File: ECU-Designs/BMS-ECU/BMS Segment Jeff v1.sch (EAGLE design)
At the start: 90 parts, among them Q10 P-CHANNEL_MOSFET_DMP3099L-7, Q11 P-CHANNEL_MOSFET_DMP3099L-7, Q12 P-CHANNEL_MOSFET_DMP3099L-7, Q13 NPN_BCP56T1, Q3 P-CHANNEL_MOSFET_DMP3099L-7, Q4 P-CHANNEL_MOSFET_DMP3099L-7, Q5 P-CHANNEL_MOSFET_DMP3099L-7, Q6 P-CHANNEL_MOSFET_DMP3099L-7, Q8 P-CHANNEL_MOSFET_DMP3099L-7, Q9 P-CHANNEL_MOSFET_DMP3099L-7

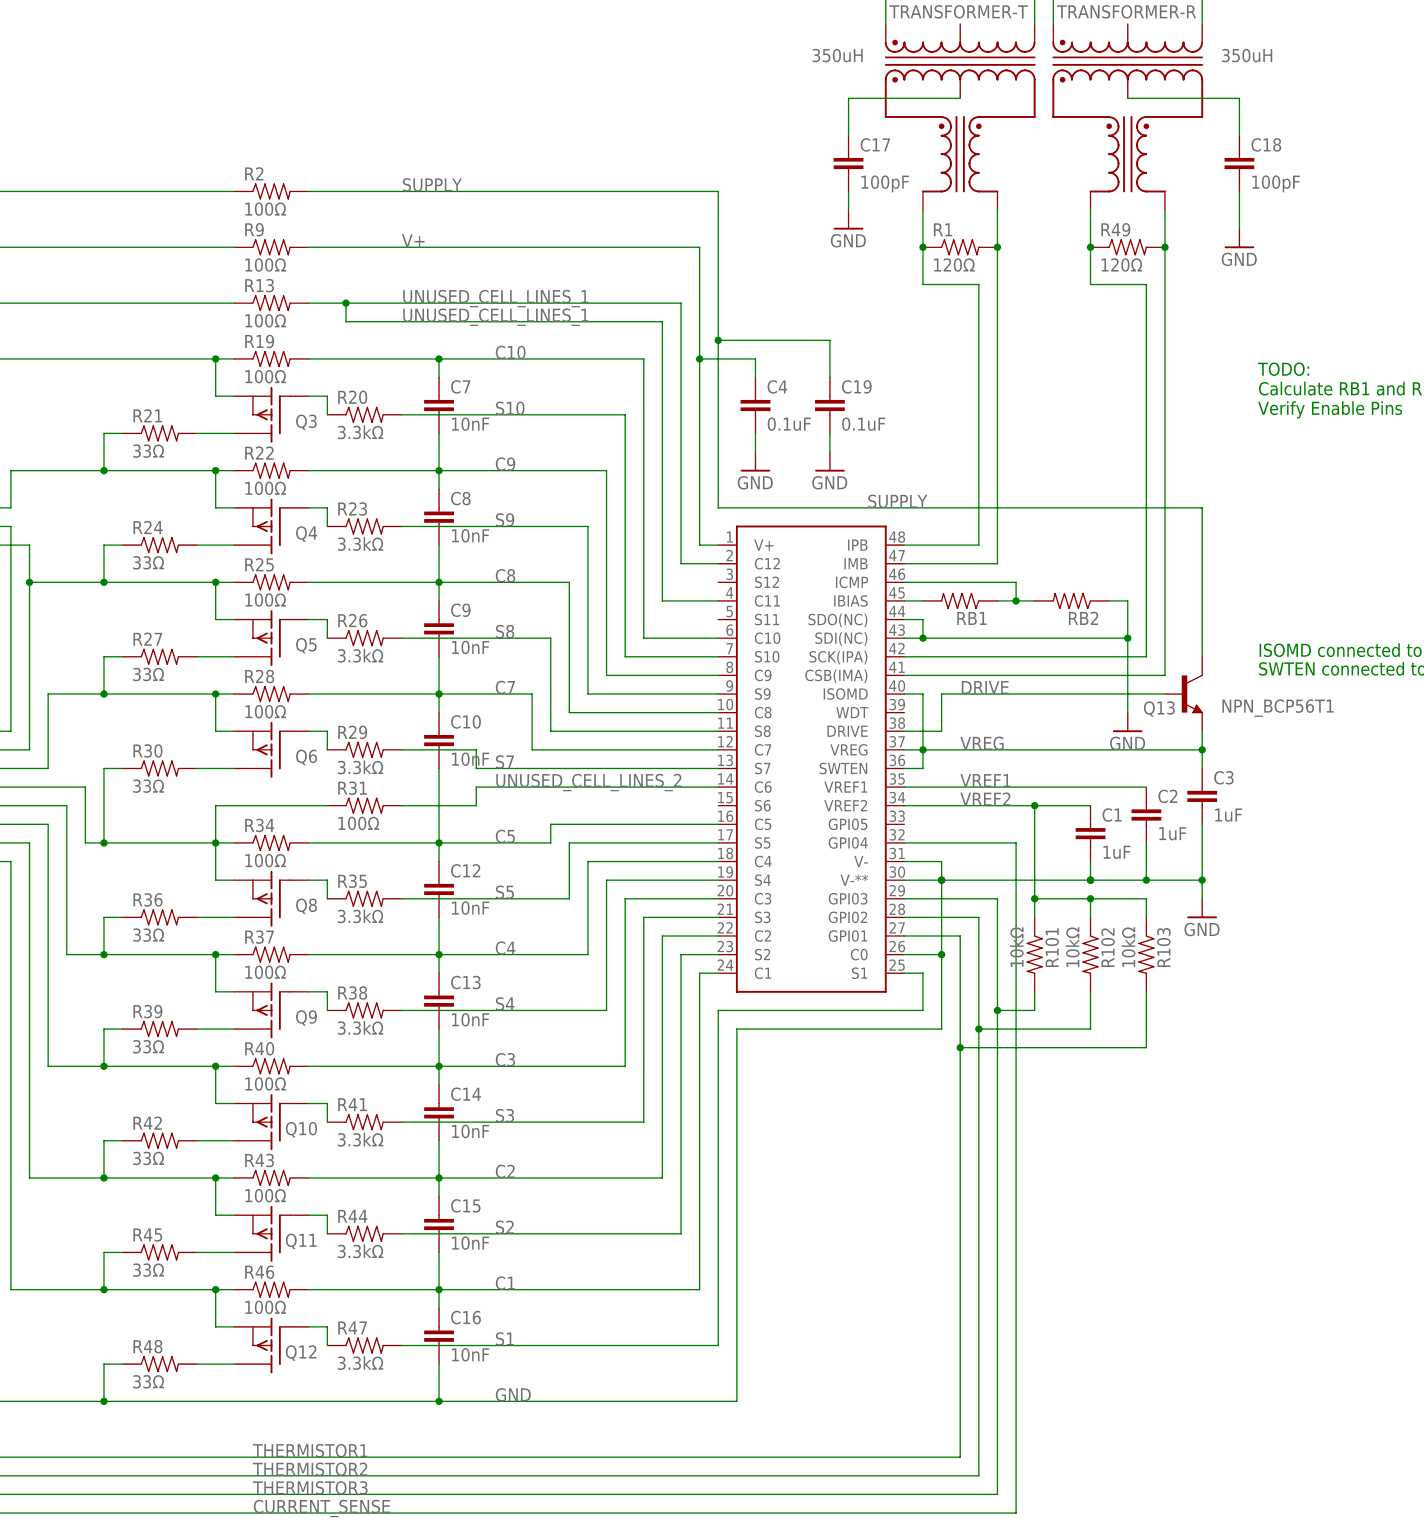
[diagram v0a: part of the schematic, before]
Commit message: Renamed components in increasing order
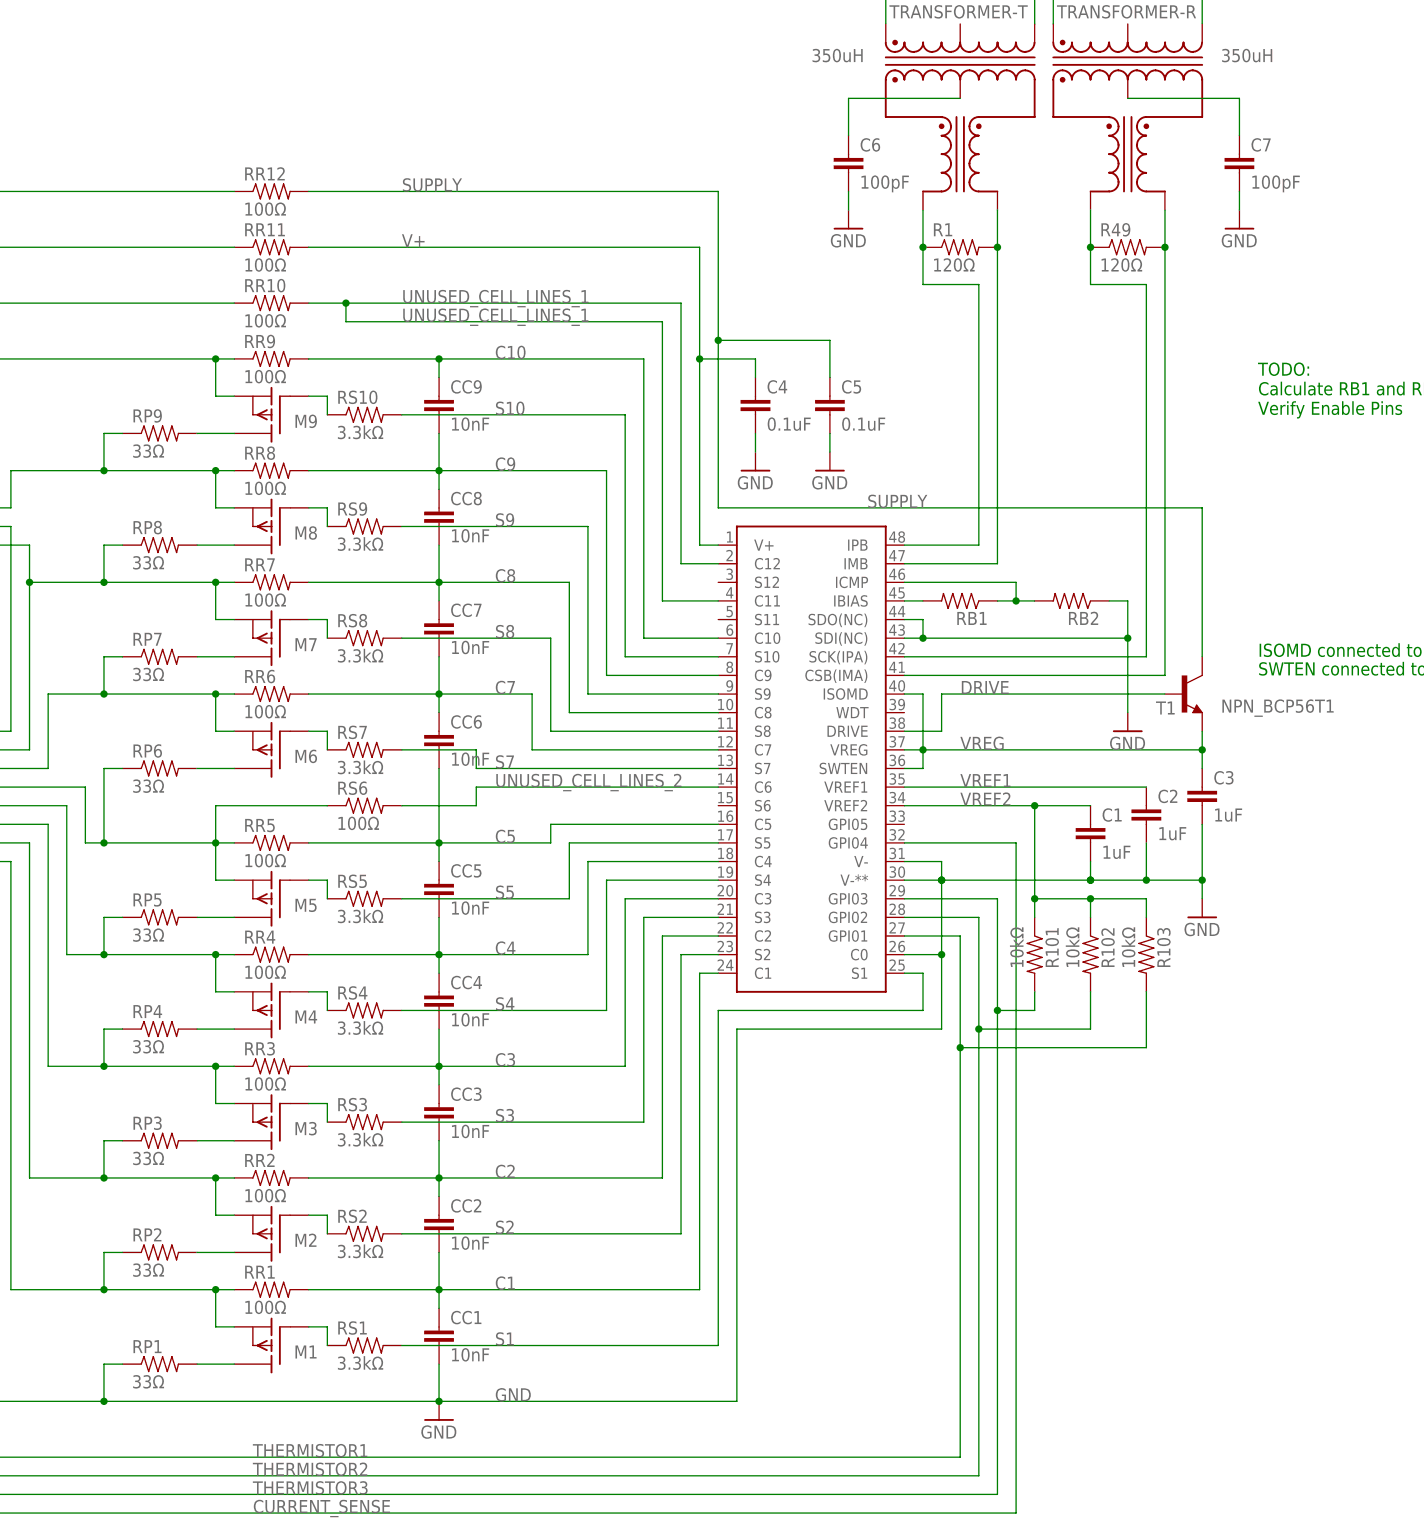
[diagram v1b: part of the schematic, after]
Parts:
- removed C18: 100pF, HyTechDevices:CAP0805
- added CC9: 10nF, HyTechDevices:CAP0805
- C7: value 10nF -> 100pF
- renumbered C10 to CC6, C12 to CC5, C13 to CC4, C14 to CC3, C15 to CC2, C16 to CC1, C17 to C6, C19 to C5, C8 to CC8, C9 to CC7, Q10 to M3, Q11 to M2, Q12 to M1, Q13 to T1, Q3 to M9, Q4 to M8, Q5 to M7, Q6 to M6, Q8 to M5, Q9 to M4, R13 to RR10, R19 to RR9, R2 to RR12, R20 to RS10, R21 to RP9, R22 to RR8, R23 to RS9, R24 to RP8, R25 to RR7, R26 to RS8, R27 to RP7, R28 to RR6, R29 to RS7, R30 to RP6, R31 to RS6, R34 to RR5, R35 to RS5, R36 to RP5, R37 to RR4, R38 to RS4, R39 to RP4, R40 to RR3, R41 to RS3, R42 to RP3, R43 to RR2, R44 to RS2, R45 to RP2, R46 to RR1, R47 to RS1, R48 to RP1, R9 to RR11
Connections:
- net C10: now also CC9.1; no longer C7.1
- net C9: now also CC9.2; no longer C7.2
- net GND: now also C7.2; no longer C18.2
- net N$1: now also C7.1; no longer C18.1
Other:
- moved on the sheet: C7

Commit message: Large changes to BMS schematic
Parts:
- removed C4, C5: 0.1uF, HyTechDevices:CAP0805
- removed CC1, CC2, CC3, CC4, CC5, CC6, CC7, CC8, CC9: 10nF, HyTechDevices:CAP0805
- removed G0, G2, G3, G4, G5, G6, G7, G8, G9: BATTERY_SPRING_KEYSTONE5222, HyTechDevices:BATTERY_SPRING_KEYSTONE5222
- removed M1, M2, M3, M4, M5, M6, M7, M8, M9: P-CHANNEL_MOSFET_DMP3099L-7, HyTechDevices:P-CHANNEL_MOSFET_DMP3099L-7
- removed RP1, RP2, RP3, RP4, RP5, RP6, RP7, RP8, RP9: 33Ω, HyTechDevices:RESISTOR2512
- removed RR1, RR10, RR11, RR12, RR2, RR3, RR4, RR5, RR6, RR7, RR8, RR9, RS6: 100Ω, HyTechDevices:RESISTOR0805-RES
- removed RS1, RS10, RS2, RS3, RS4, RS5, RS7, RS8, RS9: 3.3kΩ, HyTechDevices:RESISTOR0805-RES
- added CELL0, CELL1, CELL2, CELL3, CELL4, CELL5, CELL6, CELL7, CELL8, CELL9: BATTERY_SPRING_KEYSTONE5222, HyTechDevices:BATTERY_SPRING_KEYSTONE5222
- added CR0, CR1, CR2, CR3, CR4, CR5, CR6, CR7, CR8, CR9: 10nF, HyTechDevices:CAP0805
- added GLV_CONTROL: CPC1002N, HyTechDevices:CPC1002N
- added RC0, RC1, RC10, RC2, RC3, RC4, RC5, RC6, RC7, RC8, RC9, S1, S2: 100Ω, HyTechDevices:RESISTOR0805-RES
- added SC1, SC2: 0.1uF, HyTechDevices:CAP0805
- added X1: MINIFIT_5566-2, HyTechDevices:MINIFIT_5566-2
- G1: value BATTERY_SPRING_KEYSTONE5222 -> 100Ω; device HyTechDevices:BATTERY_SPRING_KEYSTONE5222 -> HyTechDevices:RESISTOR0805-RES
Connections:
- removed net CELL1: F1.2, M9.S, RR10.1, RR11.1, RR12.1, RR9.1, TEST_PORT-1.S
- removed net CELL2: F2.2, M8.S, RP9.1, RR8.1, TEST_PORT-2.S, TEST_PORT-3.S
- removed net CELL3: F3.2, M7.S, RP8.1, RR7.1, TEST_PORT-4.S
- removed net CELL4: F4.2, M6.S, RP7.1, RR6.1
- removed net CELL5: F5.2, M5.S, RP6.1, RR5.1, RS6.1
- removed net CELL6: F6.2, M4.S, RP5.1, RR4.1
- removed net CELL7: F7.2, M3.S, RP4.1, RR3.1
- removed net CELL8: F8.2, M2.S, RP3.1, RR2.1
- removed net CELL9: F9.2, M1.S, RP2.1, RR1.1
- removed net G0: F0.1, G0.S
- removed net G1: F1.1, G1.S
- removed net G2: F2.1, G2.S
- removed net G3: F3.1, G3.S
- removed net G4: F4.1, G4.S
- removed net G5: F5.1, G5.S
- removed net G6: F6.1, G6.S
- removed net G7: F7.1, G7.S
- removed net G8: F8.1, G8.S
- removed net G9: F9.1, G9.S
- removed net N$15: M9.G, RS10.1
- removed net N$18: M9.D, RP9.2
- removed net N$20: M5.G, RS5.1
- removed net N$22: M4.G, RS4.1
- removed net N$25: M8.D, RP8.2
- removed net N$27: M3.G, RS3.1
- removed net N$28: M2.G, RS2.1
- removed net N$29: M1.G, RS1.1
- removed net N$30: M7.D, RP7.2
- removed net N$36: M6.D, RP6.2
- removed net N$43: M5.D, RP5.2
- removed net N$51: M4.D, RP4.2
- removed net N$53: M3.D, RP3.2
- removed net N$61: M2.D, RP2.2
- removed net N$66: M1.D, RP1.2
- removed net N$68: M8.G, RS9.1
- removed net N$69: M7.G, RS8.1
- removed net N$70: M6.G, RS7.1
- removed net UNUSED_CELL_LINES_1: RR10.2, U$2.C11, U$2.C12
- removed net UNUSED_CELL_LINES_2: RS6.2, U$2.C6
- new net C0: CR0.1, CR1.2, RC0.2, U$2.C0
- new net C11: U$2.C11
- new net C12: U$2.C12
- new net C6: CR6.1, CR7.2, RC6.2, U$2.C6
- new net CC0: CELL0.S, F0.1
- new net CC1: CELL1.S, F1.1
- new net CC2: CELL2.S, F2.1
- new net CC3: CELL3.S, F3.1
- new net CC4: CELL4.S, F4.1
- new net CC5: CELL5.S, F5.1
- new net CC6: CELL6.S, F6.1
- new net CC7: CELL7.S, F7.1
- new net CC8: CELL8.S, F8.1
- new net CC9: CELL9.S, F9.1
- new net N$10: G1.1, GLV_CONTROL.CONTROL-
- new net N$11: GLV_CONTROL.CONTROL+, X1-1.S
- new net N$3: GLV_CONTROL.DC-, S1.1, S2.1
- new net S11: U$2.S11
- new net S12: U$2.S12
- new net S6: U$2.S6
- new net SENSE1: F1.2, TEST_PORT-2.S
- new net SENSE1_J: RC1.1, TEST_PORT-4.S
- new net SENSE2: F2.2, RC2.1
- new net SENSE3: F3.2, RC3.1
- new net SENSE4: F4.2, RC4.1
- new net SENSE5: F5.2, RC5.1
- new net SENSE6: F6.2, RC6.1
- new net SENSE7: F7.2, RC7.1
- new net SENSE8: F8.2, RC8.1
- new net SENSE9: F9.2, GLV_CONTROL.DC+, RC10.1, RC9.1
- new net V-: C1.2, C2.2, C3.2, C6.2, C7.2, CR0.2, F0.2, RB2.1, RC0.1, SC1.2, SC2.2, TEST_PORT-3.S, U$2.SDI(NC), U$2.SDO(NC), U$2.V-, U$2.V-**
- net C1: now also CR1.1, CR2.2, RC1.2; no longer CC1.1, CC2.2, RR1.2
- net C10: now also RC10.2; no longer CC9.1, RR9.2
- net C2: now also CR2.1, CR3.2, RC2.2; no longer CC2.1, CC3.2, RR2.2
- net C3: now also CR3.1, CR4.2, RC3.2; no longer CC3.1, CC4.2, RR3.2
- net C4: now also CR4.1, CR5.2, RC4.2; no longer CC4.1, CC5.2, RR4.2
- net C5: now also CR5.1, CR6.2, RC5.2; no longer CC5.1, CC6.2, RR5.2
- net C7: now also CR7.1, CR8.2, RC7.2; no longer CC6.1, CC7.2, RR6.2
- net C8: now also CR8.1, CR9.2, RC8.2; no longer CC7.1, CC8.2, RR7.2
- net C9: now also CR9.1, RC9.2; no longer CC8.1, CC9.2, RR8.2
- net GND: now also G1.2, X1-2.S; no longer C1.2, C2.2, C3.2, C4.2, C5.2, C6.2, C7.2, CC1.2, F0.2, RB2.1, RP1.1, U$2.C0, U$2.SDI(NC), U$2.SDO(NC), U$2.V-, U$2.V-**
- net S1: no longer RS1.2
- net S10: no longer RS10.2
- net S2: no longer RS2.2
- net S3: no longer RS3.2
- net S4: no longer RS4.2
- net S5: no longer RS5.2
- net S7: no longer RS7.2
- net S8: no longer RS8.2
- net S9: no longer RS9.2
- net SUPPLY: now also S1.2, SC1.1; no longer C5.1, RR12.2
- net V+: now also S2.2, SC2.1; no longer C4.1, RR11.2
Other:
- note added: "Also connects to: C11 C12"
- note added: "Gate Drive"
- note added: "See LTC6804-1 DATASHEET pg.61"
- note added: "See pg. 67 for unused cells (9 cells per LTC6804 in this design)"
- note removed: "Is this 10th fuse necessary?"
- moved on the sheet: F0, F1, F2, F3, F4, F5, F6, F7, F8, F9, SENSE_LINES-1, SENSE_LINES-2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

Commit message: Small detailed changes to BMS (negative) schematic
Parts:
- added X2: To Positive BMS, HyTechDevices:MINIFIT_5566-2
- RB1, RB2: value (none) -> 1.2k
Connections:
- net CC9: now also X2-1.S, X2-2.S
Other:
- moved on the sheet: C1, C2, C3, R101, R102, R103, T1

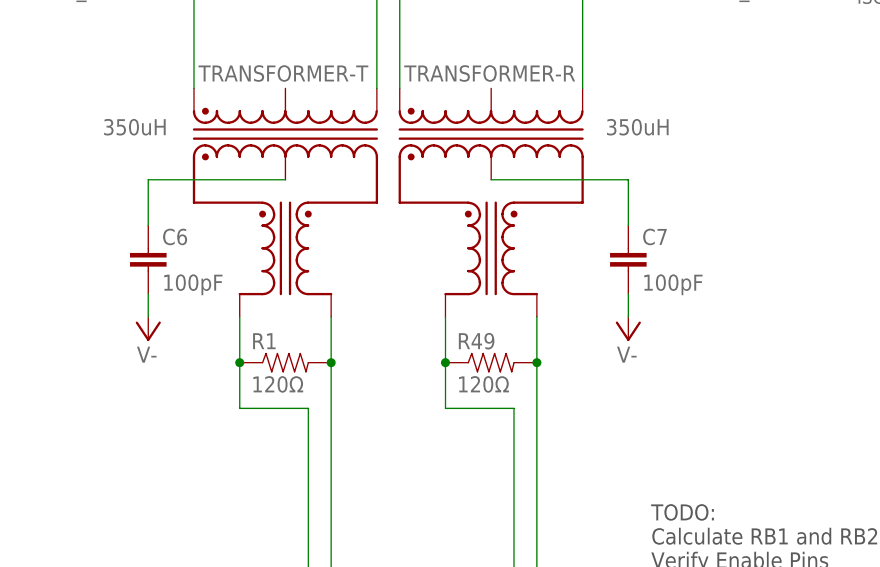
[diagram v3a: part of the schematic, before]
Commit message: Mega BMS Progress (Negative side board layout)
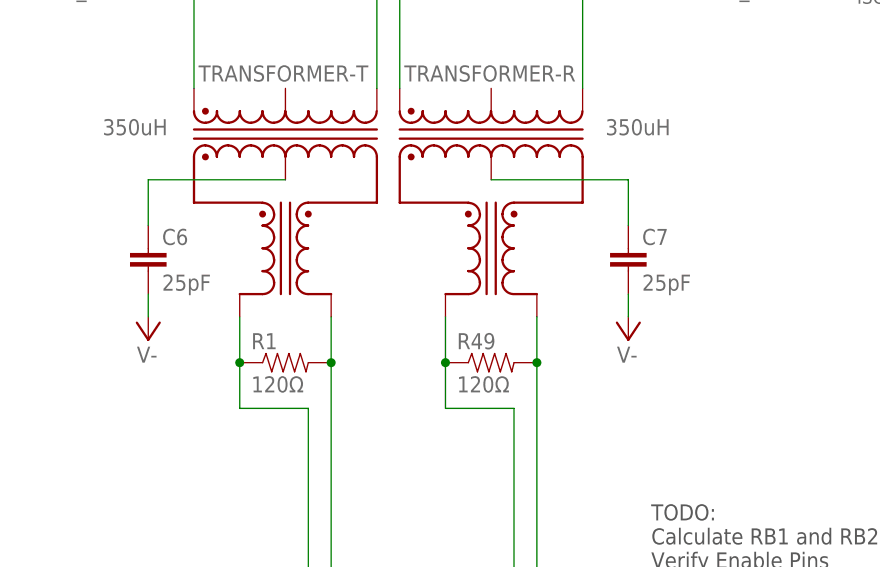
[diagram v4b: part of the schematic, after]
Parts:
- C6, C7: value 100pF -> 25pF
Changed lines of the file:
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@@
 <?xml version="1.0" encoding="utf-8"?>
 <!DOCTYPE eagle SYSTEM "eagle.dtd">
-<eagle version="8.0.2">
+<eagle version="8.1.0">
 <drawing>
 <settings>
@@
 <setting verticaltext="up"/>
 </settings>
-<grid distance="0.1" unitdist="inch" unit="inch" style="lines" multiple="1" display="no" altdistance="0.05" altunitdist="inch" altunit="inch"/>
+<grid distance="0.1" unitdist="inch" unit="inch" style="lines" multiple="1" display="no" altdistance="0.01" altunitdist="inch" altunit="inch"/>
 <layers>
 <layer number="1" name="Top" color="4" fill="1" visible="no" active="no"/>
@@
 <part name="U$2" library="HyTechDevices" deviceset="LTC6804-1" device=""/>
 <part name="R1" library="HyTechDevices" deviceset="RESISTOR" device="0805-RES" value="120Ω"/>
-<part name="C6" library="HyTechDevices" deviceset="CAP" device="0805" value="100pF"/>
-<part name="C7" library="HyTechDevices" deviceset="CAP" device="0805" value="100pF"/>
+<part name="C6" library="HyTechDevices" deviceset="CAP" device="0805" value="25pF"/>
+<part name="C7" library="HyTechDevices" deviceset="CAP" device="0805" value="25pF"/>
 <part name="S1" library="HyTechDevices" deviceset="RESISTOR" device="0805-RES" value="100Ω"/>
 <part name="SC2" library="HyTechDevices" deviceset="CAP" device="0805" value="0.1uF"/>

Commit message: More BMS trace updates
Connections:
- net N$10 renamed SSR-
- net N$11 renamed SSR+
- net N$3 renamed SUPPLY_INTER
- net CC9: no longer X2-1.S, X2-2.S
- net SENSE9: now also X2-1.S, X2-2.S
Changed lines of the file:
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@@
 <wire x1="-213.36" y1="114.3" x2="-213.36" y2="66.04" width="0.1524" layer="91"/>
 <wire x1="-213.36" y1="66.04" x2="-213.36" y2="40.64" width="0.1524" layer="91"/>
-<wire x1="-213.36" y1="40.64" x2="-259.08" y2="40.64" width="0.1524" layer="91"/>
+<wire x1="-213.36" y1="40.64" x2="-256.54" y2="40.64" width="0.1524" layer="91"/>
 <pinref part="F9" gate="G$1" pin="2"/>
 <label x="-248.92" y="40.64" size="1.778" layer="95"/>
 <portref moduleinst="DRAIN9" port="CELL+"/>
+<wire x1="-256.54" y1="40.64" x2="-259.08" y2="40.64" width="0.1524" layer="91"/>
 <wire x1="-180.34" y1="66.04" x2="-213.36" y2="66.04" width="0.1524" layer="91"/>
 <junction x="-213.36" y="66.04"/>
@@
 <wire x1="-213.36" y1="114.3" x2="-167.64" y2="114.3" width="0.1524" layer="91"/>
 <wire x1="-167.64" y1="114.3" x2="-167.64" y2="119.38" width="0.1524" layer="91"/>
+<pinref part="X2" gate="-1" pin="S"/>
+<wire x1="-289.56" y1="55.88" x2="-287.02" y2="55.88" width="0.1524" layer="91"/>
+<pinref part="X2" gate="-2" pin="S"/>
+<wire x1="-289.56" y1="58.42" x2="-287.02" y2="58.42" width="0.1524" layer="91"/>
+<wire x1="-287.02" y1="58.42" x2="-287.02" y2="55.88" width="0.1524" layer="91"/>
+<wire x1="-287.02" y1="55.88" x2="-256.54" y2="55.88" width="0.1524" layer="91"/>
+<wire x1="-256.54" y1="55.88" x2="-256.54" y2="40.64" width="0.1524" layer="91"/>
+<junction x="-287.02" y="55.88"/>
+<junction x="-256.54" y="40.64"/>
 </segment>
 </net>
@@
 <net name="CC9" class="0">
 <segment>
-<wire x1="-289.56" y1="40.64" x2="-287.02" y2="40.64" width="0.1524" layer="91"/>
 <pinref part="F9" gate="G$1" pin="1"/>
 <pinref part="CELL9" gate="G$1" pin="S"/>
 <label x="-281.94" y="40.64" size="1.778" layer="95"/>
-<pinref part="X2" gate="-1" pin="S"/>
-<wire x1="-287.02" y1="40.64" x2="-269.24" y2="40.64" width="0.1524" layer="91"/>
-<wire x1="-289.56" y1="55.88" x2="-287.02" y2="55.88" width="0.1524" layer="91"/>
-<wire x1="-287.02" y1="55.88" x2="-287.02" y2="40.64" width="0.1524" layer="91"/>
-<junction x="-287.02" y="40.64"/>
-<pinref part="X2" gate="-2" pin="S"/>
-<wire x1="-289.56" y1="58.42" x2="-287.02" y2="58.42" width="0.1524" layer="91"/>
-<wire x1="-287.02" y1="58.42" x2="-287.02" y2="55.88" width="0.1524" layer="91"/>
-<junction x="-287.02" y="55.88"/>
+<wire x1="-289.56" y1="40.64" x2="-269.24" y2="40.64" width="0.1524" layer="91"/>
 </segment>
 </net>
@@
 </segment>
 </net>
-<net name="N$3" class="0">
+<net name="SUPPLY_INTER" class="0">
 <segment>
 <pinref part="GLV_CONTROL" gate="G$1" pin="DC-"/>
@@
 </segment>
 </net>
-<net name="N$10" class="0">
-<segment>
-<pinref part="GLV_CONTROL" gate="G$1" pin="CONTROL-"/>
-<pinref part="G1" gate="G$1" pin="1"/>
-<wire x1="-162.56" y1="139.7" x2="-162.56" y2="142.24" width="0.1524" layer="91"/>
-<wire x1="-162.56" y1="142.24" x2="-157.48" y2="142.24" width="0.1524" layer="91"/>
-</segment>
-</net>
-<net name="N$11" class="0">
+<net name="SSR+" class="0">
 <segment>
 <pinref part="X1" gate="-1" pin="S"/>
@@
 </segment>
 </net>
+<net name="SSR-" class="0">
+<segment>
+<pinref part="GLV_CONTROL" gate="G$1" pin="CONTROL-"/>
+<pinref part="G1" gate="G$1" pin="1"/>
+<wire x1="-162.56" y1="139.7" x2="-162.56" y2="142.24" width="0.1524" layer="91"/>
+<wire x1="-162.56" y1="142.24" x2="-157.48" y2="142.24" width="0.1524" layer="91"/>
+</segment>
+</net>
